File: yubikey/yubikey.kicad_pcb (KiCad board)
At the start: 4 copper layers, 18.5 x 45 mm, 31 parts, among them J1 USB_C_Receptacle_USB2.0_16P, SW1 BOOTSEC, SW2 RESET, U1 ATECC608A-SSHDA, U2 RP2040, U3 W25Q128JVS, Y1 12MHz

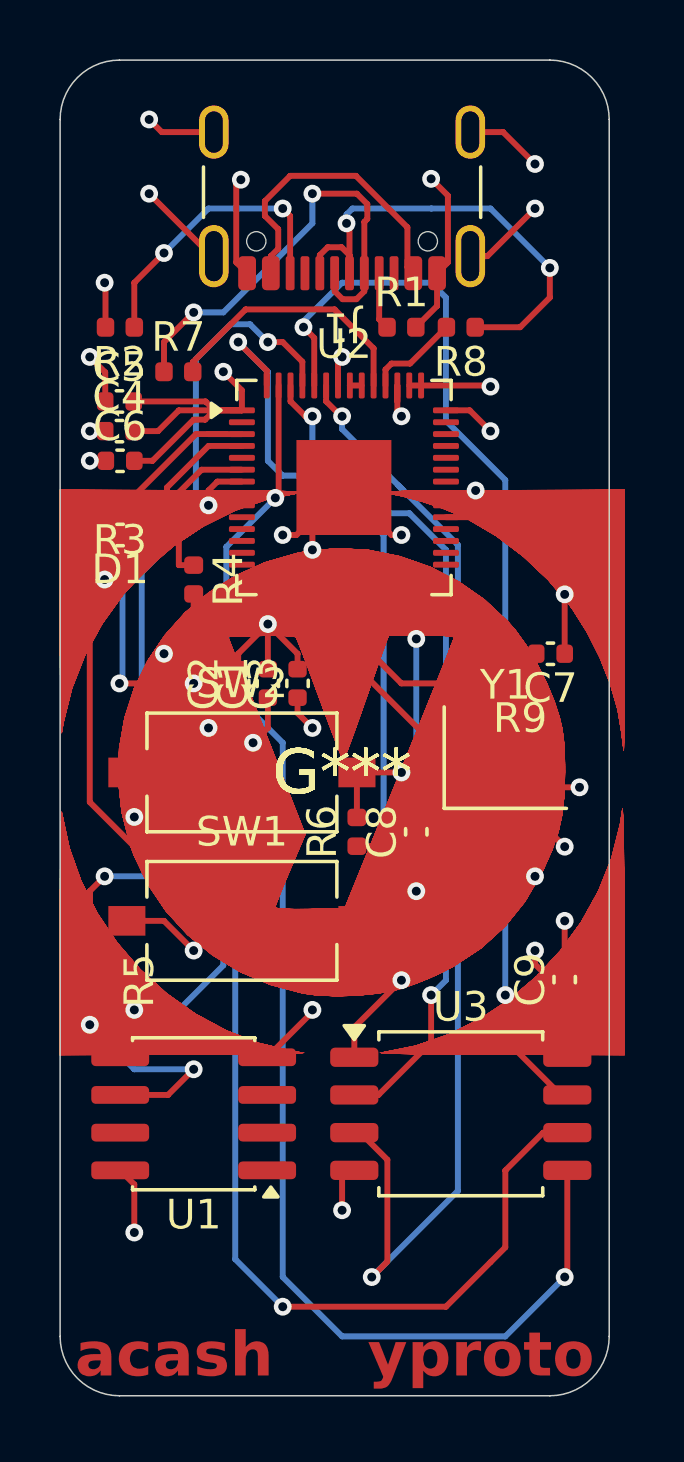
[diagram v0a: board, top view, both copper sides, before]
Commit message: fixed some issues with pcb
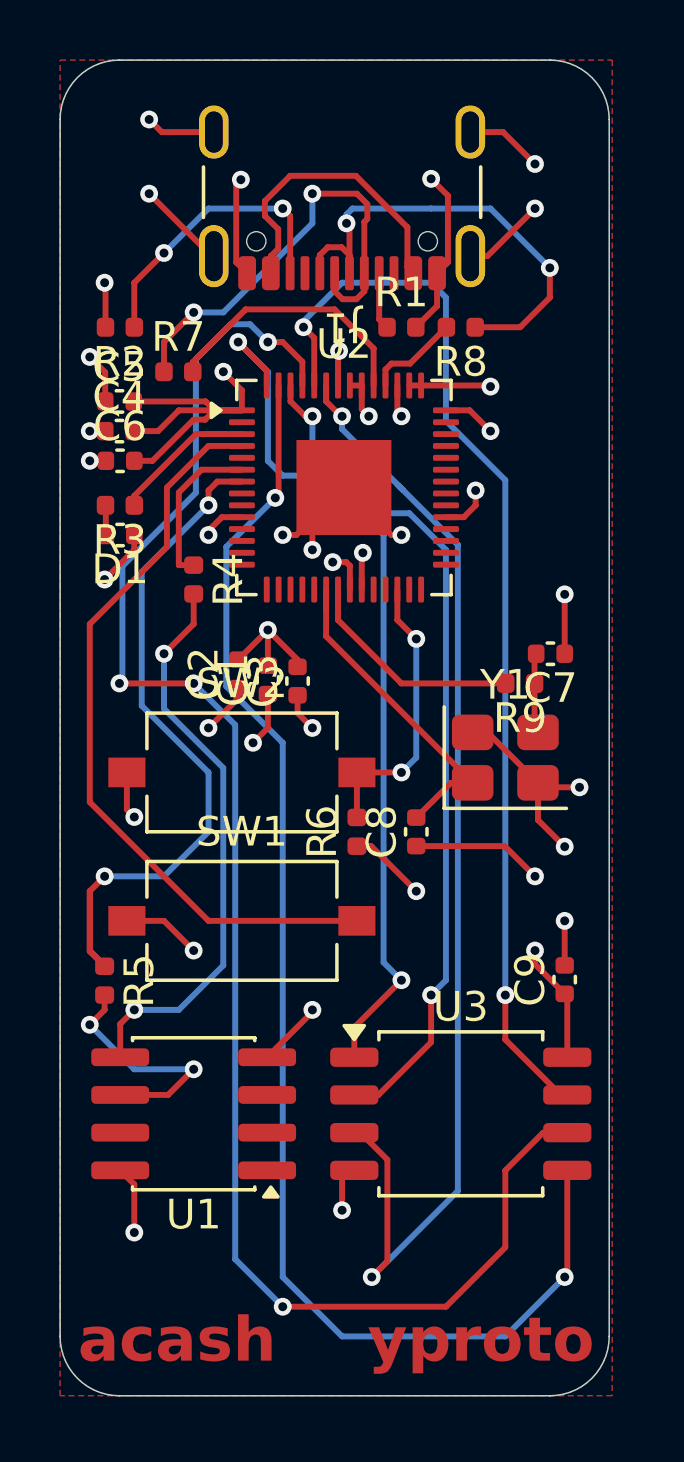
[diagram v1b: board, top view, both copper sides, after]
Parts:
- removed G*** (x5): LOGO, yubico:yubico
- moved C2 0.32 mm to (121.0, 120.7)
- moved C1 0.12 mm to (122.0, 120.9)
- moved C3 0.08 mm to (123.0, 120.9)
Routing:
- net +3V3: track 28.4 -> 32.3 mm, vias 7 -> 10
- net Earth: track 61.5 -> 62.1 mm
- net +1V1: track 8.04 -> 7.79 mm, vias 3 -> 4
- added copper zone on F.Cu, net +1V1
